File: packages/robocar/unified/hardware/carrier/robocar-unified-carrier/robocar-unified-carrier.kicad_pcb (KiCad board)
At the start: 2 copper layers, 100 x 100 mm, 55 parts, among them J1 IDC 2x7 head cable, J11 Test: 3V3 5V GND VBAT, J12 Test: GND SDA SCL RST, J13 GND post, J14 GND post, J15 UART0 TX tap, J16 IDC 2x7 head cable, J17 IDC 2x7 head cable, J18 GPIO A/B, J2 IDC 2x7 head cable, J3 XT30 pack in, J4 LM2596 module, J5 Motor left, J6 Motor right, J7 RCWL-1601 front, J8 RCWL-1601 rear, J9 SSD1306 0.91in, U1 XIAO ESP32-S3 Sense, U2 AMS1117-3.3, U3 XIAO ESP32-S3 Sense, U4 XIAO ESP32-S3 Sense

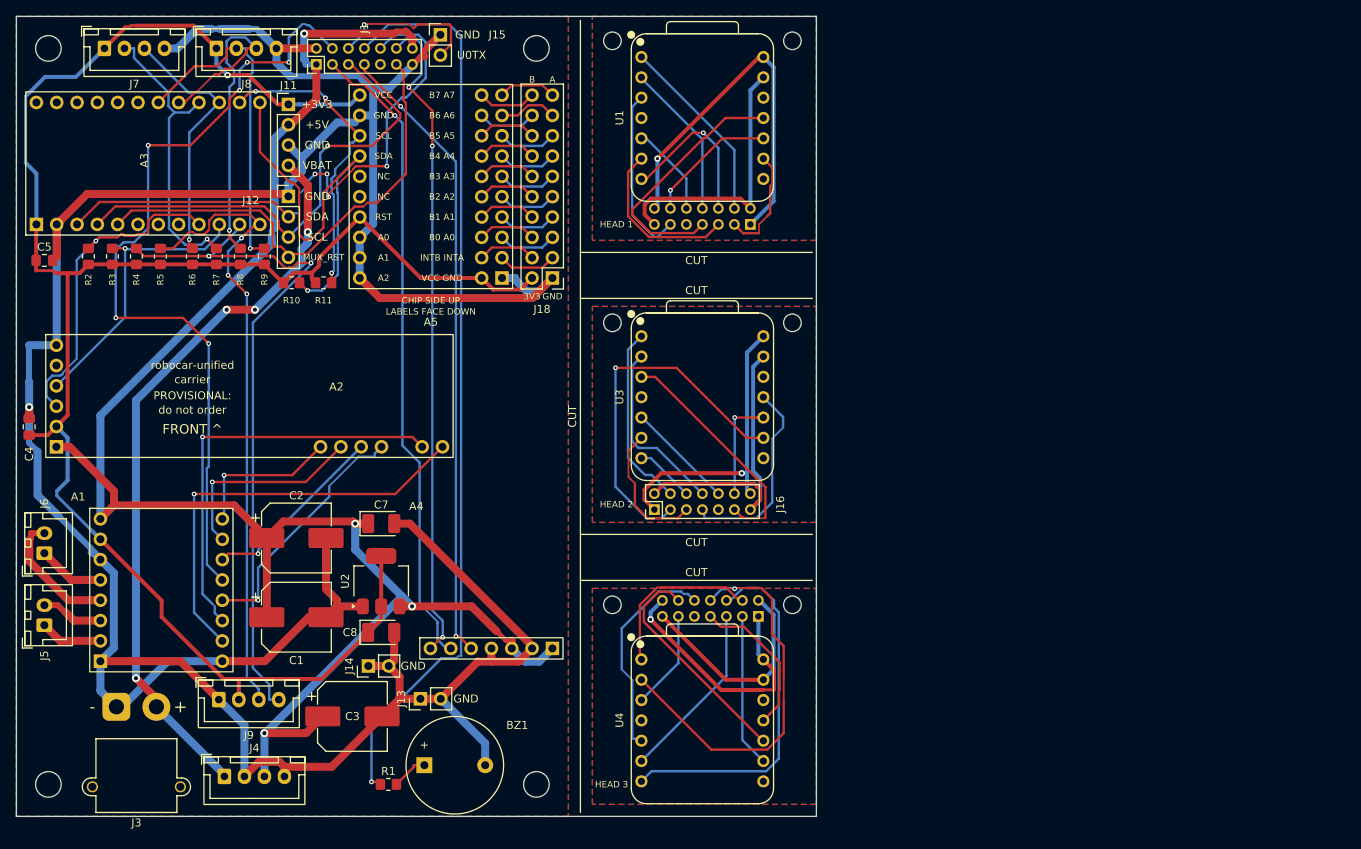
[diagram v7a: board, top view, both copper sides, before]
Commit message: feat(robocar-unified): backport the integrated carrier's pre-fab review fixes (#812)
Works through #810's ten findings on the socketed carrier:

- [fanout] with required vias on the bulk capacitors, C4, C5 and the
  AMS1117 and its capacitors: GND vias go from 1 to 11, and no SMD
  ground pad is left without one
- F1, a 3 A hold, 16 V 1812 PTC (C883162) between the XT30 and VBAT;
  the harness keeps its unfused VBAT rail
- mux channel pull-ups R2-R11 from 10 kOhm to 2.2 kOhm (C17520, Basic)
  for the 300 ns Fast-mode rise time; the harness docs follow
- head 2's top saw band reaches 1 mm past its cut; head 3's stays at
  0.5 mm, because a wider band left HEAD3_PIEZO unroutable past J17
- silkscreen at 1.0 mm where DRC allows it
- README records each finding's outcome, including the not-applicable
  ones (cutoff, LED brightness, decoupling distance); WIRING.md gains
  the low-battery and 5 V current-budget notes from SNVS124G

Board re-placed and re-routed; every carrier gate passes and the stamp
is rewritten.


Claude-Session: https://claude.ai/code/session_01HMYrZm6JVcVgRypdr4Jojz

Co-authored-by: Claude <noreply@anthropic.com>
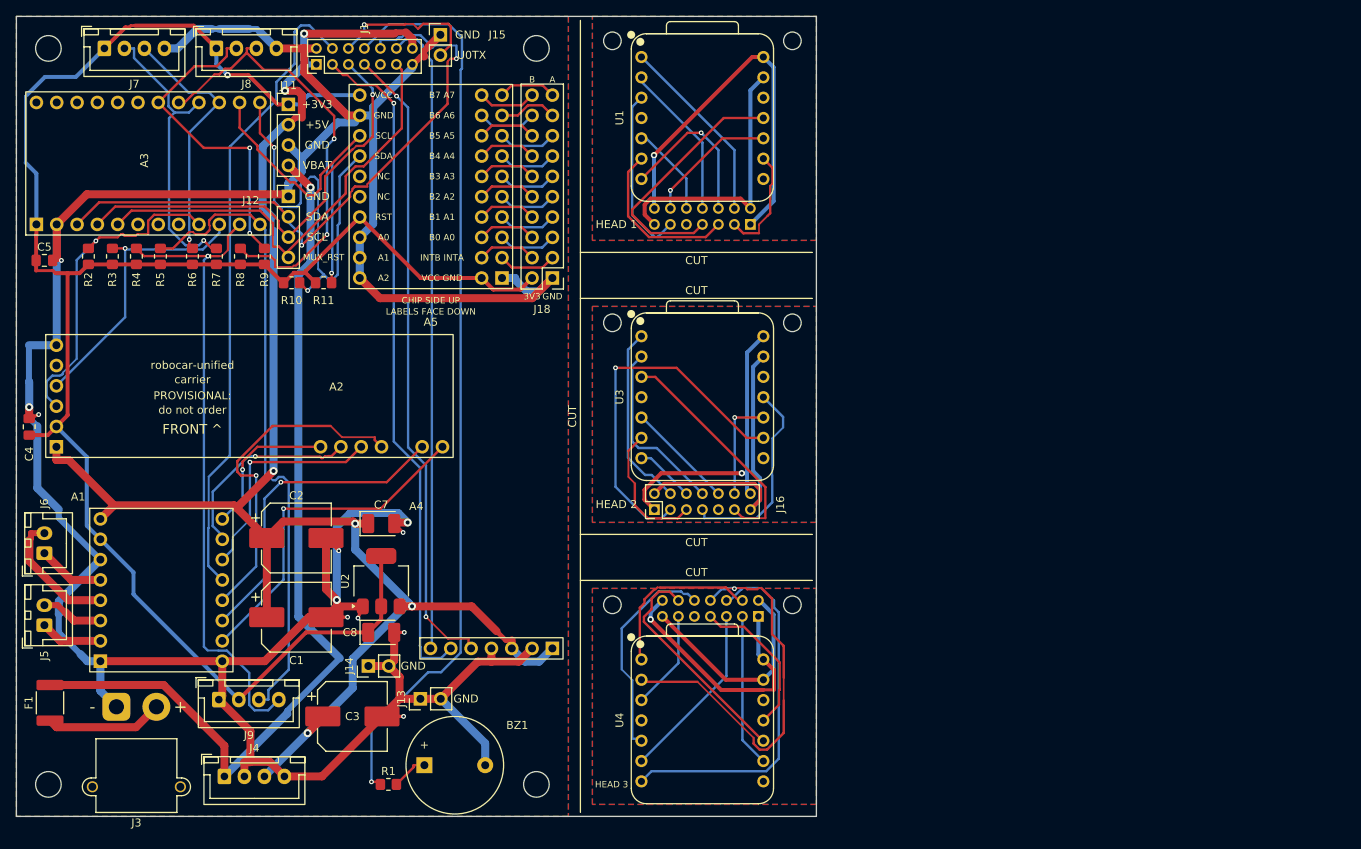
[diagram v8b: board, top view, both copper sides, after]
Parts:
- added F1: 3A hold 16V, Fuse:Fuse_1812_4532Metric_Pad1.30x3.40mm_HandSolder, F.Cu at (104.2, 185.8)
- R10, R11, R2, R3, R4, R5, R6, R7, R8, R9: value 10k -> 2.2k
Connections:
- J3 pad 2: VBAT -> PACK_IN
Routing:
- net VBAT: track 93.0 -> 115.1 mm, vias 4 -> 1
- net MOTOR_STBY: track 101.8 -> 80.0 mm, vias 6 -> 0
- net PACK_IN: track 0.00 -> 14.7 mm
- net BIN2: track 51.9 -> 39.8 mm
- net CH4_SDA: track 44.4 -> 56.3 mm, vias 1 -> 2
- net BIN1: track 31.2 -> 42.3 mm
- net +5V: track 221.2 -> 210.4 mm, vias 4 -> 6
- net PWMB: track 53.3 -> 42.8 mm
- net CH1_SDA: track 88.5 -> 80.6 mm, vias 2 -> 1
- net CH2_SCL: track 38.4 -> 45.9 mm, vias 3 -> 1
- net I2C_SCL: track 60.4 -> 54.6 mm
- net AIN1: track 23.5 -> 28.3 mm
- net I2C_SDA: track 73.8 -> 78.6 mm, vias 4 -> 2
- net I2S_BCLK: track 80.3 -> 84.7 mm
- net MUX_RST: track 59.4 -> 56.8 mm
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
